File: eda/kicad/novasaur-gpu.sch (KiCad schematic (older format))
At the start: 21 parts, among them U1 74F86, U28 74F163, U29 74F163, U3 74F08, U30 74F541, U31 74F574, U32 74F574, U33 74F541, U34 74F574, U35 74F299, U36 74F574, U37 74F157

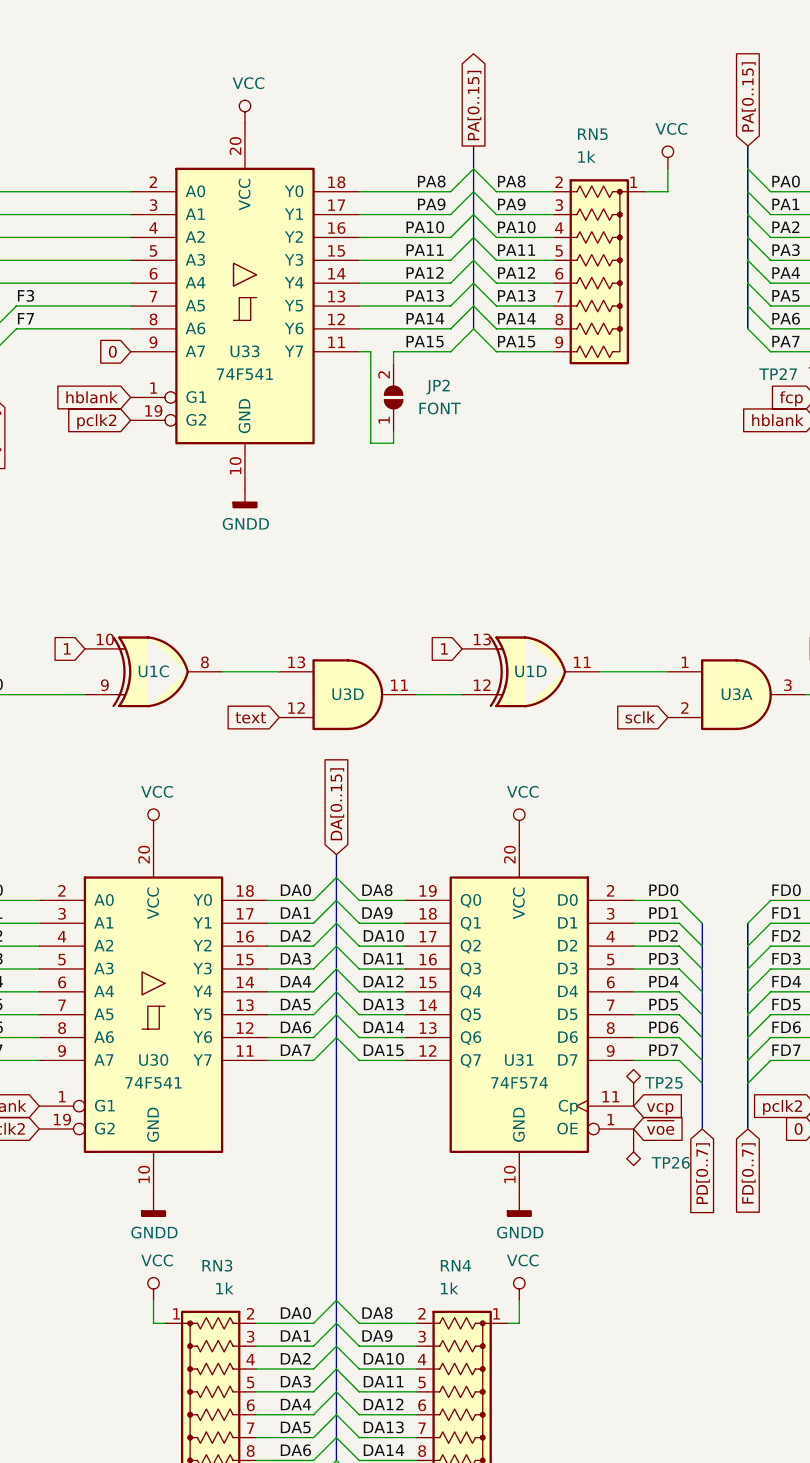
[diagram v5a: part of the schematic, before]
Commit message: audio muting and updated filter/inverting amplifier
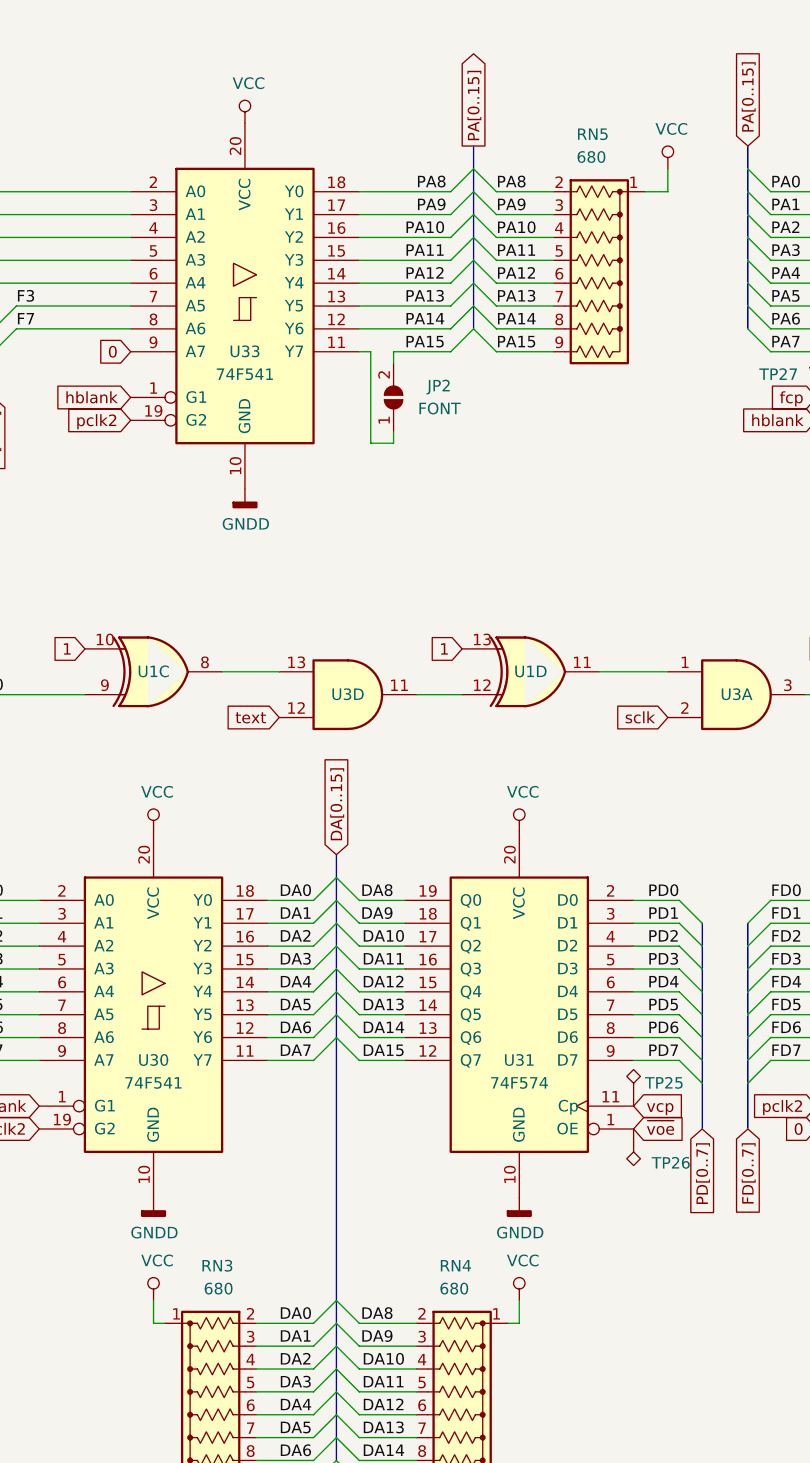
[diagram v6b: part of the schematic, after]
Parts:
- RN2, RN3, RN4: value 1k -> 680
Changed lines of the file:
@@
 Sheet 3 4
 Title "Graphics Processing Unit"
-Date "2020-09-10"
+Date "2020-10-01"
 Rev "1.7"
 Comp ""
@@
 AR Path="/5DA1E9BD/5D1C9541" Ref="RN5"  Part="1"
 F 0 "RN5" V 5100 1850 50  0000 L CNN
-F 1 "1k" V 5200 1850 50  0000 L CNN
+F 1 "680" V 5200 1850 50  0000 L CNN
 F 2 "Resistor_THT:R_Array_SIP9" V 6225 1950 50  0001 C CNN
 F 3 "http://www.vishay.com/docs/31509/csc.pdf" H 5750 1950 50  0001 C CNN
@@
 AR Path="/5DA1E9BD/5D1C1190" Ref="RN4"  Part="1"
 F 0 "RN4" V 4500 6800 50  0000 L CNN
-F 1 "1k" V 4600 6800 50  0000 L CNN
+F 1 "680" V 4600 6800 50  0000 L CNN
 F 2 "Resistor_THT:R_Array_SIP9" V 5625 6900 50  0001 C CNN
 F 3 "http://www.vishay.com/docs/31509/csc.pdf" H 5150 6900 50  0001 C CNN
@@
 AR Path="/5DA1E9BD/5D1C1196" Ref="RN3"  Part="1"
 F 0 "RN3" V 3400 6800 50  0000 L CNN
-F 1 "1k" V 3500 6800 50  0000 L CNN
+F 1 "680" V 3500 6800 50  0000 L CNN
 F 2 "Resistor_THT:R_Array_SIP9" V 4525 6900 50  0001 C CNN
 F 3 "http://www.vishay.com/docs/31509/csc.pdf" H 4050 6900 50  0001 C CNN

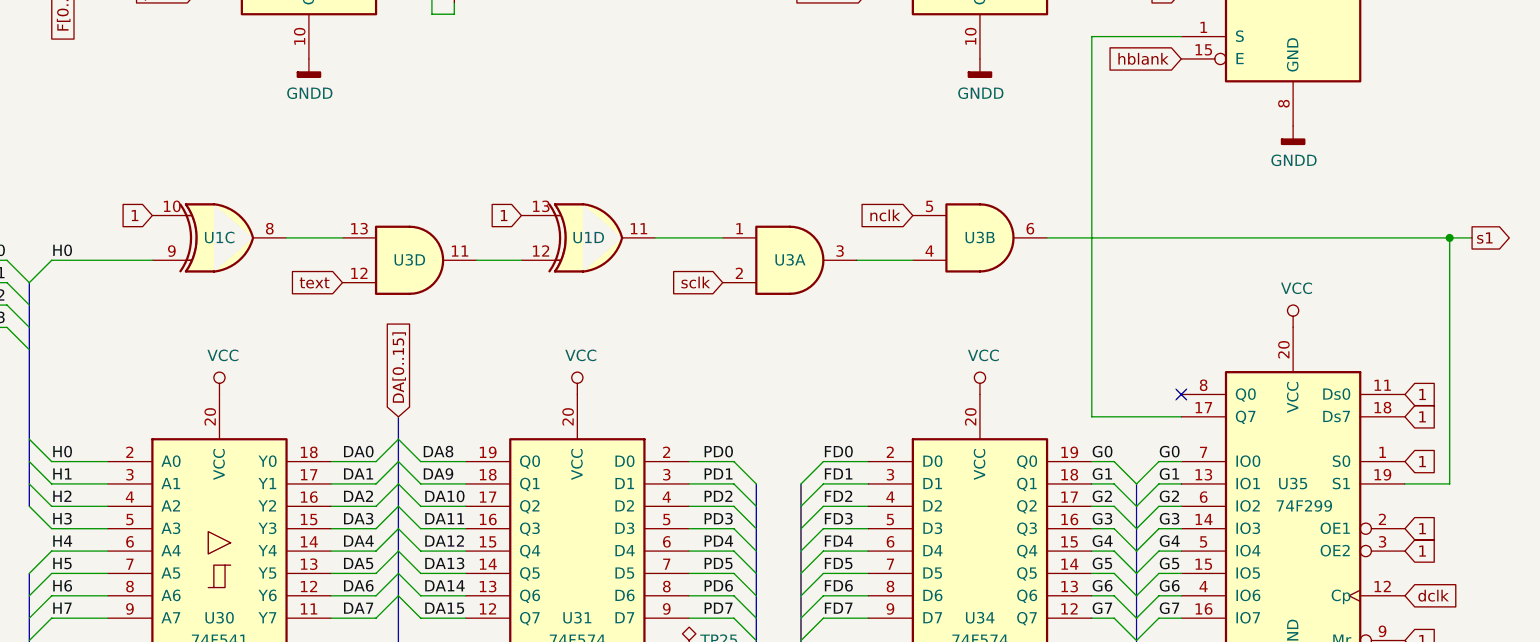
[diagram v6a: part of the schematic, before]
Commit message: rev 8 schematic stop FCP during blanking
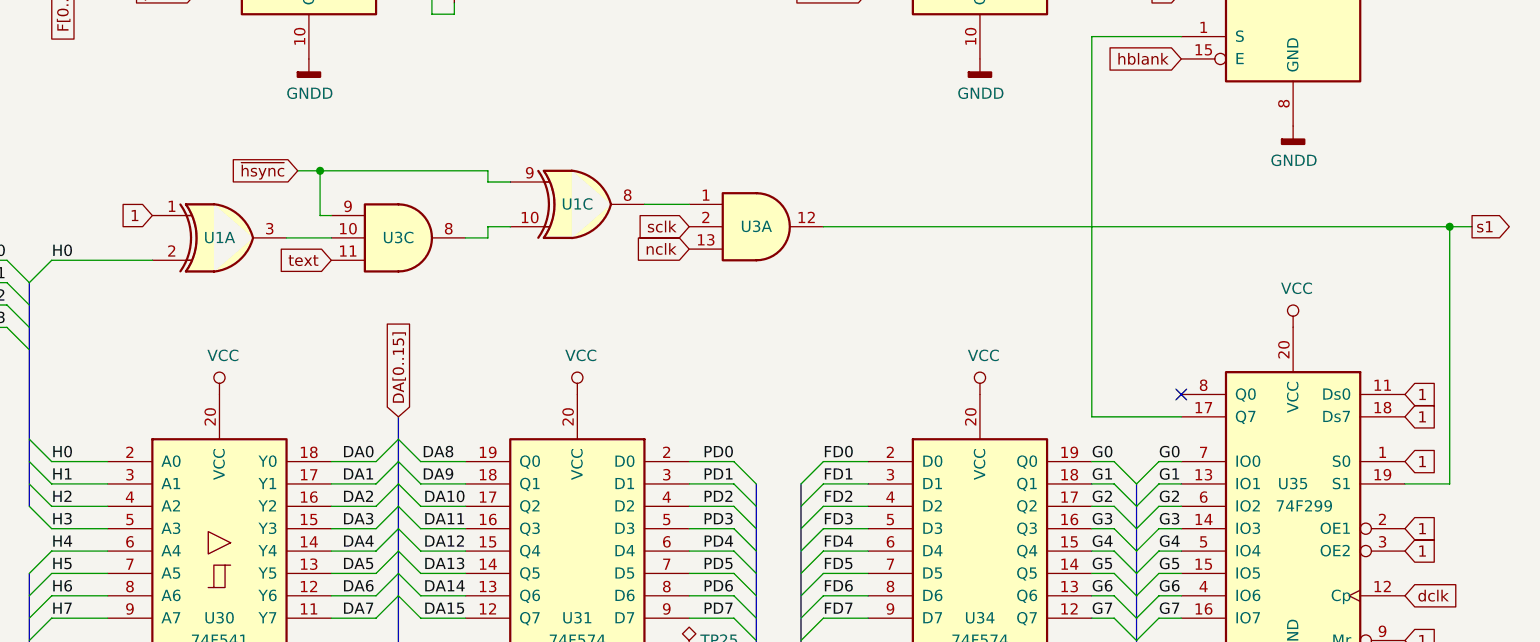
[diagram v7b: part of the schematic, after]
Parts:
- removed unit 4 of U1
- removed U3: 74F08, Package_DIP:DIP-14_W7.62mm_LongPads, symbol 74xx:74LS08
- added unit 1 of U1
- added U3: 74F11, Package_DIP:DIP-14_W7.62mm_LongPads, symbol 74xx:74LS11
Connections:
- net 1: now also U1.1; no longer U1.10
- net H0: now also U1.2; no longer U1.9
- net nclk: now also U3.13
- net s1: now also U3.12
- net sclk: now also U3.2
- net text: now also U3.11
- net ~hsync: now also U1.9, U3.9
- net at U1.8: now also U3.1
- new net: U1.10, U3.8
- new net: U1.3, U3.10
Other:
- moved on the sheet: U1C
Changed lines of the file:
@@
 Sheet 3 4
 Title "Graphics Processing Unit"
-Date "2020-10-01"
-Rev "1.7"
+Date "2020-10-10"
+Rev "1.8"
 Comp ""
 Comment1 "(c) A J Hewitt 2020"
@@
 	1    0    0    -1
 $EndComp
-Text GLabel 4350 3850 0    50   Input ~ 0
+Text GLabel 4300 3750 0    50   Input ~ 0
 text
 Text GLabel 1700 3850 0    50   Input ~ 0
@@
 Entry Wire Line
 	6100 5350 6200 5450
-Text GLabel 6900 3550 0    50   Input ~ 0
+Text GLabel 5900 3700 0    50   Input ~ 0
 nclk
-Text GLabel 6050 3850 0    50   Input ~ 0
+Text GLabel 5900 3600 0    50   Input ~ 0
 sclk
 Text Label 3050 3750 0    50   ~ 0
@@
 Text GLabel 6700 5550 0    50   Input ~ 0
 pclk2
-Text GLabel 9400 3650 2    50   Output ~ 0
+Text GLabel 9400 3600 2    50   Output ~ 0
 s1
 Text GLabel 5900 5650 2    50   Input ~ 0
@@
 Wire Wire Line
 	1500 2150 1700 2150
-$Comp
-L 74xx:74LS08 U?
-U 2 1 5DCE5E0A
-P 7200 3650
-AR Path="/5CDEEC9F/5DCE5E0A" Ref="U?"  Part="2"
-AR Path="/5DAA5CD8/5DCE5E0A" Ref="U?"  Part="2"
-AR Path="/5DCE5E0A" Ref="U?"  Part="2"
-AR Path="/5DA1E9BD/5DCE5E0A" Ref="U3"  Part="2"
-F 0 "U3" H 7200 3650 50  0000 C CNN
-F 1 "74F08" H 7200 3850 50  0001 C CNN
-F 2 "Package_DIP:DIP-14_W7.62mm_LongPads" H 7200 3650 50  0001 C CNN
-F 3 "http://www.ti.com/lit/gpn/sn74LS08" H 7200 3650 50  0001 C CNN
-	2    7200 3650
-	1    0    0    1
-$EndComp
-$Comp
-L 74xx:74LS08 U?
-U 1 1 5DCE5E10
-P 6350 3750
-AR Path="/5CDEEC9F/5DCE5E10" Ref="U?"  Part="1"
-AR Path="/5DAA5CD8/5DCE5E10" Ref="U?"  Part="1"
-AR Path="/5DCE5E10" Ref="U?"  Part="1"
-AR Path="/5DA1E9BD/5DCE5E10" Ref="U3"  Part="1"
-F 0 "U3" H 6350 3750 50  0000 C CNN
-F 1 "74F08" H 6350 3550 50  0001 C CNN
-F 2 "Package_DIP:DIP-14_W7.62mm_LongPads" H 6350 3750 50  0001 C CNN
-F 3 "http://www.ti.com/lit/gpn/sn74LS08" H 6350 3750 50  0001 C CNN
-	1    6350 3750
-	1    0    0    -1
-$EndComp
 $Comp
 L Connector:TestPoint_Alt TP?
@@
 Text GLabel 1700 4750 0    50   Input ~ 0
 1
-Wire Wire Line
-	9300 3650 9400 3650
 $Comp
 L 74xx:74LS157 U?
@@
 Text GLabel 9100 2450 2    50   Output ~ 0
 ~hsync
-Text GLabel 5150 3550 0    50   Input ~ 0
-1
-$Comp
-L 74xx:74LS86 U?
-U 4 1 5E72FE45
-P 5450 3650
-AR Path="/5E72FE45" Ref="U?"  Part="4"
-AR Path="/5DA1E9BD/5E72FE45" Ref="U1"  Part="4"
-AR Path="/5DA1E9BA/5E72FE45" Ref="U?"  Part="4"
-F 0 "U1" H 5450 3650 50  0000 C CNN
-F 1 "74F86" H 5450 3884 50  0001 C CNN
-F 2 "Package_DIP:DIP-14_W7.62mm_LongPads" H 5450 3650 50  0001 C CNN
-F 3 "74xx/74ls86.pdf" H 5450 3650 50  0001 C CNN
-	4    5450 3650
-	1    0    0    1
-$EndComp
-$Comp
-L 74xx:74LS08 U?
-U 4 1 5E79B5B5
-P 4650 3750
-AR Path="/5DAA3954/5E79B5B5" Ref="U?"  Part="4"
-AR Path="/5DAA5CD8/5E79B5B5" Ref="U?"  Part="4"
-AR Path="/5E79B5B5" Ref="U?"  Part="4"
-AR Path="/5DA1E9BD/5E79B5B5" Ref="U3"  Part="4"
-AR Path="/5DA1E9C0/5E79B5B5" Ref="U?"  Part="4"
-F 0 "U3" H 4650 3750 50  0000 C CNN
-F 1 "74F08" H 4650 3550 50  0001 C CNN
-F 2 "Package_DIP:DIP-14_W7.62mm_LongPads" H 4650 3750 50  0001 C CNN
-F 3 "http://www.ti.com/lit/gpn/sn74LS08" H 4650 3750 50  0001 C CNN
-	4    4650 3750
-	1    0    0    1
-$EndComp
 Wire Wire Line
 	3050 3750 3500 3750
-Wire Wire Line
-	4950 3750 5150 3750
 Text GLabel 2700 2250 2    50   Output ~ 0
 ~kbdtx
@@
 L 74xx:74LS86 U?
 U 3 1 5F723456
-P 3800 3650
+P 5400 3500
 AR Path="/5F723456" Ref="U?"  Part="3"
 AR Path="/5DA1E9BD/5F723456" Ref="U1"  Part="3"
+F 0 "U1" H 5400 3500 50  0000 C CNN
+F 1 "74F86" H 5400 3734 50  0001 C CNN
+F 2 "Package_DIP:DIP-14_W7.62mm_LongPads" H 5400 3500 50  0001 C CNN
+F 3 "74xx/74ls86.pdf" H 5400 3500 50  0001 C CNN
+	3    5400 3500
+	1    0    0    -1
+$EndComp
+Text GLabel 3500 3550 0    50   Input ~ 0
+1
+$Comp
+L 74xx:74LS11 U3
+U 1 1 5F83CB24
+P 6200 3600
+F 0 "U3" H 6200 3600 50  0000 C CNN
+F 1 "74F11" H 6200 3834 50  0001 C CNN
+F 2 "Package_DIP:DIP-14_W7.62mm_LongPads" H 6200 3600 50  0001 C CNN
+F 3 "http://www.ti.com/lit/gpn/sn74LS11" H 6200 3600 50  0001 C CNN
+	1    6200 3600
+	1    0    0    -1
+$EndComp
+Text GLabel 4150 3350 0    50   Input ~ 0
+~hsync
+Wire Wire Line
+	4300 3550 4250 3550
+Wire Wire Line
+	4250 3350 4150 3350
+Wire Wire Line
+	4900 3650 5000 3650
+Wire Wire Line
+	5000 3350 4250 3350
+Connection ~ 4250 3350
+Wire Wire Line
+	4250 3350 4250 3550
+$Comp
+L 74xx:74LS11 U?
+U 3 1 5FA63205
+P 4600 3650
+AR Path="/5FA63205" Ref="U?"  Part="3"
+AR Path="/5DA1E9BD/5FA63205" Ref="U3"  Part="3"
+F 0 "U3" H 4600 3650 50  0000 C CNN
+F 1 "74F11" H 4600 3884 50  0001 C CNN
+F 2 "Package_DIP:DIP-14_W7.62mm_LongPads" H 4600 3650 50  0001 C CNN
+F 3 "http://www.ti.com/lit/gpn/sn74LS11" H 4600 3650 50  0001 C CNN
+	3    4600 3650
+	1    0    0    -1
+$EndComp
+Wire Wire Line
+	9300 3600 9300 4750
+Connection ~ 9300 3600
+Wire Wire Line
+	9300 3600 9400 3600
+Wire Wire Line
+	5100 3600 5000 3600
+Wire Wire Line
+	5000 3600 5000 3650
+Wire Wire Line
+	5100 3400 5000 3400
+Wire Wire Line
+	5000 3400 5000 3350
+$Comp
+L 74xx:74LS86 U1
+U 1 1 5F8424E4
+P 3800 3650
 F 0 "U1" H 3800 3650 50  0000 C CNN
 F 1 "74F86" H 3800 3884 50  0001 C CNN
 F 2 "Package_DIP:DIP-14_W7.62mm_LongPads" H 3800 3650 50  0001 C CNN
 F 3 "74xx/74ls86.pdf" H 3800 3650 50  0001 C CNN
-	3    3800 3650
-	1    0    0    1
-$EndComp
-Text GLabel 3500 3550 0    50   Input ~ 0
-1
-Wire Wire Line
-	9300 3650 9300 4750
-Connection ~ 9300 3650
-Wire Wire Line
-	4100 3650 4350 3650
-Wire Wire Line
-	6650 3750 6900 3750
-Wire Wire Line
-	7500 3650 9300 3650
-Wire Wire Line
-	5750 3650 6050 3650
+	1    3800 3650
+	1    0    0    -1
+$EndComp
+Wire Wire Line
+	4100 3650 4300 3650
+Wire Wire Line
+	5700 3500 5900 3500
+Wire Wire Line
+	6500 3600 9300 3600
 Wire Bus Line
 	3100 2150 3100 2450

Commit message: rev 8 updates
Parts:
- added TP23: ~VBLANK, TestPoint:TestPoint_Pad_1.0x1.0mm, symbol Connector:TestPoint_Alt
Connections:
- net ~hsync: no longer U1.9, U3.9
- net vblank: no longer names the net of U32.13 (Q6)
- net vblank: now also U1.9, U3.9, TP23.1
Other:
- moved on the sheet: JP2, RN5, TP24
